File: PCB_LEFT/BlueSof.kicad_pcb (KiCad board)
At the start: 2 copper layers, 134.8 x 98.3 mm, 88 parts, among them J1 USB_C_Receptacle_USB2.0, J12 SM02B-SRSS-TB_LF__SN_, Q2 A03407, SW1 SW_PUSH, SW10 SW_PUSH, SW11 SW_PUSH, SW12 SW_PUSH, SW13 SW_PUSH, SW14 SW_PUSH, SW15 SW_PUSH, SW16 SW_PUSH, SW17 SW_PUSH, SW18 SW_PUSH, SW19 SW_PUSH, SW2 SW_PUSH, SW20 SW_PUSH, SW21 SW_PUSH, SW22 SW_PUSH, SW23 SW_PUSH, SW24 SW_PUSH, SW25 Rotary_Encoder_Switch, SW26 SW_PUSH, SW27 SW_PUSH, SW28 SW_PUSH, SW3 SW_PUSH, SW4 SW_PUSH, SW5 SW_PUSH, SW6 SW_PUSH, SW7 SW_PUSH, SW8 SW_PUSH, SW9 SW_PUSH, U1 LN2054Y42AMR, U2 E73-2G4M08S1C, U3 AP2112K-3.3, Y1 32.768kHz

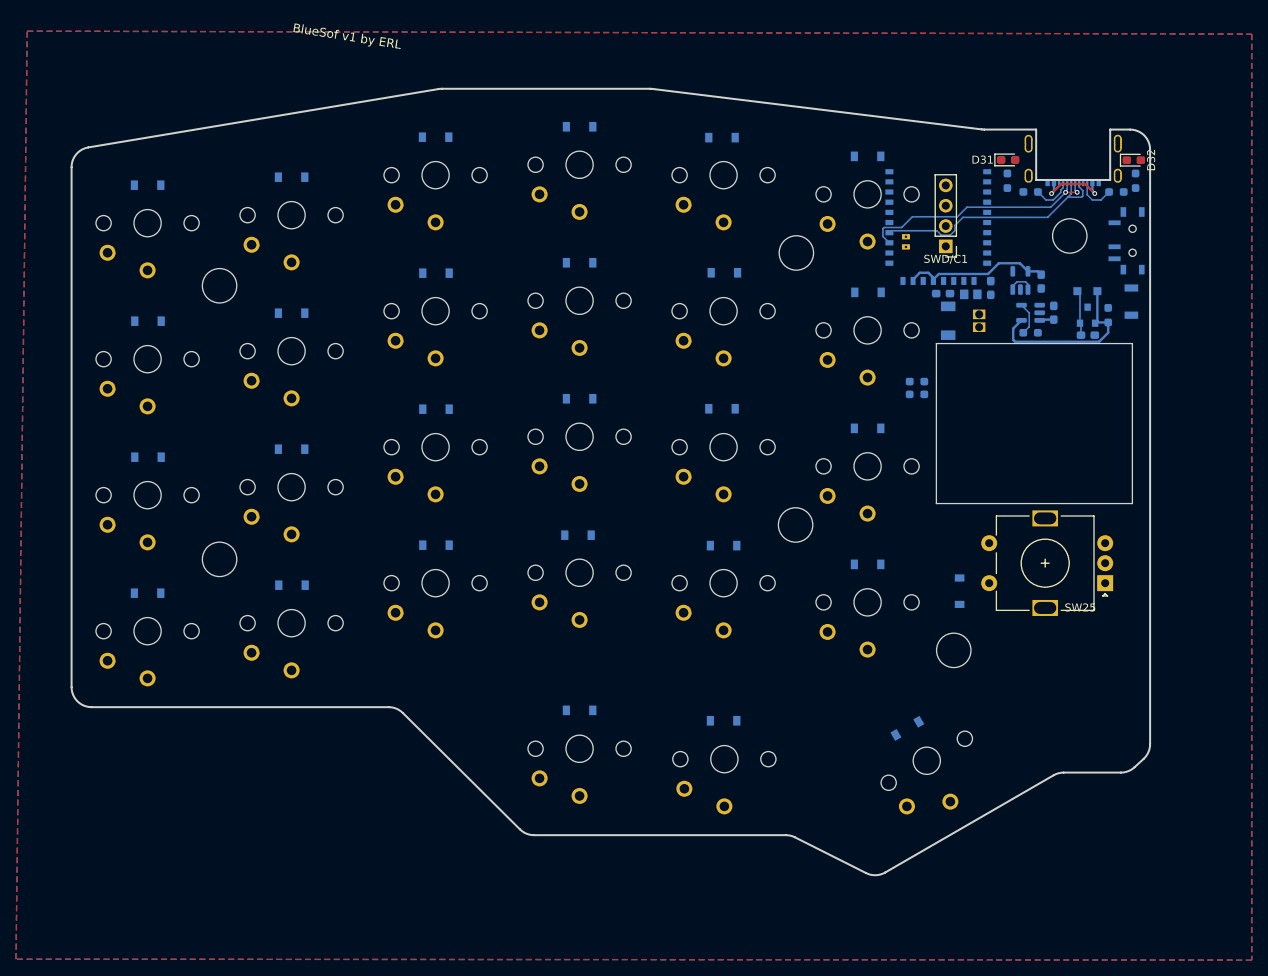
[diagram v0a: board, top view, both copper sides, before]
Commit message: ordered left side from jlc
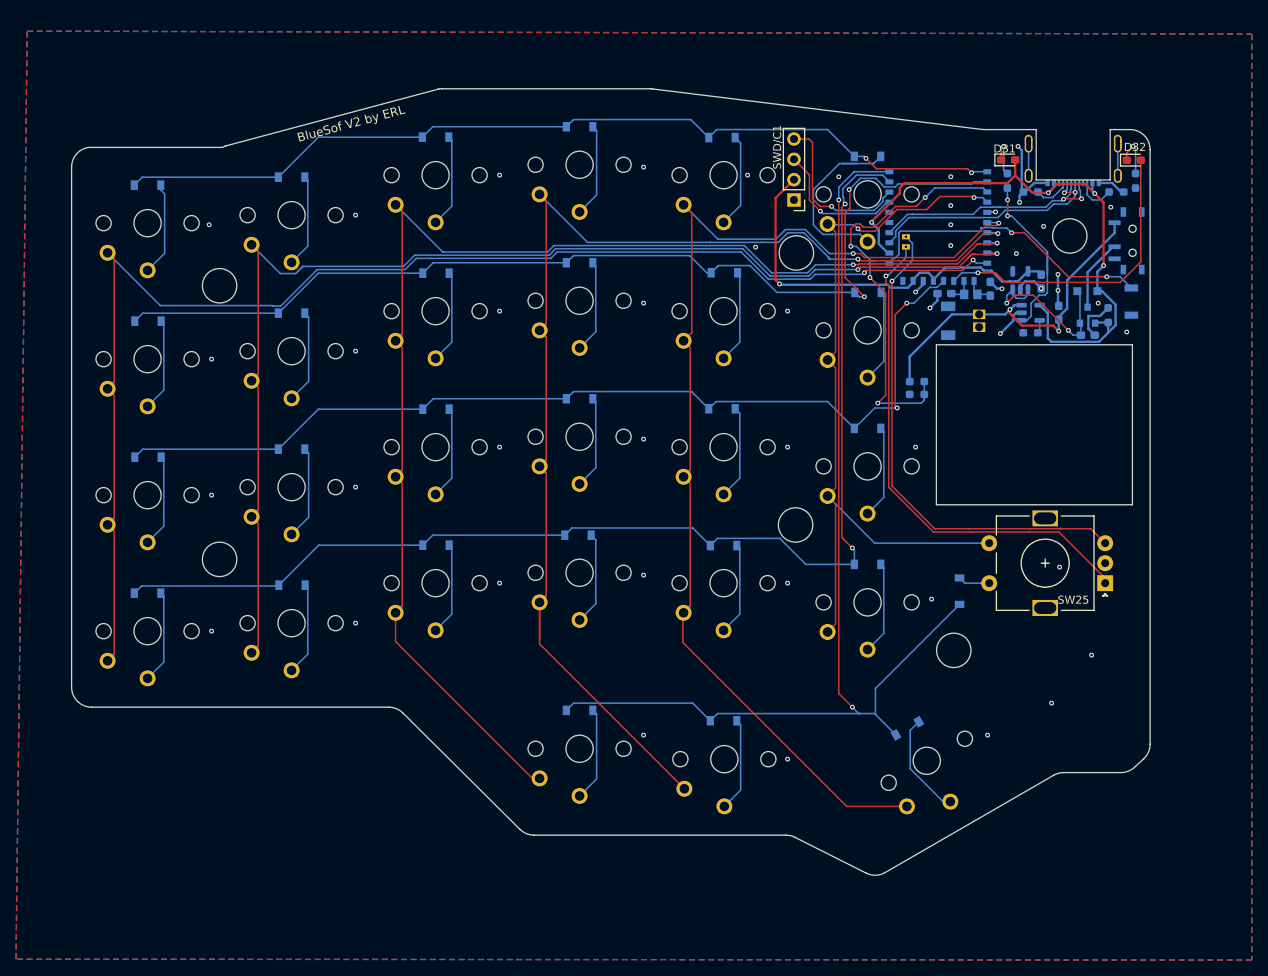
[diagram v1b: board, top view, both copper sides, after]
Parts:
- J12: value SM02B-SRSS-TB_LF__SN_ -> SM02B-SRSS-TB(LF)(SN)
- moved SWD/C1 19.8 mm to (175.7, 54.8)
- moved C4 5.93 mm to (200.2, 65.9), turned to -90 degrees
- moved C3 5.84 mm to (194.5, 66.5), turned to 0 degrees
- moved C1 0.62 mm to (208.8, 68.9)
- turned D7 to 0 degrees
- turned R1 to -90 degrees
- turned R2 to 180 degrees
- turned R6 to -90 degrees
- turned U1 to 0 degrees
- turned Y1 to 0 degrees
- renumbered BATT1 to BATT_SW, RESET1 to RESET
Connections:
- net DATA+ renamed D+
- net DATA- renamed D-
- BATT_SW pad 3: no_connect_72 -> unconnected-(BATT1-Pad3)
- H1 pad 1: Net-(H1-Pad1) -> unconnected-(H1-Pad1)
- H2 pad 1: Net-(H2-Pad1) -> unconnected-(H2-Pad1)
- H3 pad 1: Net-(H3-Pad1) -> unconnected-(H3-Pad1)
- H4 pad 1: Net-(H4-Pad1) -> unconnected-(H4-Pad1)
- H5 pad 1: Net-(H5-Pad1) -> unconnected-(H5-Pad1)
- H6 pad 1: Net-(H6-Pad1) -> unconnected-(H6-Pad1)
- J1 pad A8: no_connect_73 -> unconnected-(J1-PadA8)
- J1 pad B8: no_connect_74 -> unconnected-(J1-PadB8)
- J1 pad S1: GND -> unconnected-(J1-PadS1)
- U2 pad 33: Net-(U2-Pad33) -> unconnected-(U2-Pad33)
- U2 pad 35: Net-(U2-Pad35) -> unconnected-(U2-Pad35)
- U3 pad 4: no_connect_87 -> unconnected-(U3-Pad4)
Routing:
- net col0: track 0.00 -> 171.1 mm, vias 0 -> 2
- net col2: track 0.00 -> 164.4 mm, vias 0 -> 2
- net col1: track 0.00 -> 154.4 mm, vias 0 -> 2
- net col3: track 0.00 -> 154.1 mm, vias 0 -> 2
- net row3: track 0.00 -> 150.8 mm, vias 0 -> 2
- net col4: track 0.00 -> 139.9 mm, vias 0 -> 2
- net row4: track 0.00 -> 136.2 mm, vias 0 -> 2
- net row1: track 0.00 -> 131.0 mm, vias 0 -> 2
- net row2: track 0.00 -> 122.0 mm, vias 0 -> 2
- net row0: track 0.00 -> 113.6 mm, vias 0 -> 2
- net col5: track 0.00 -> 98.5 mm, vias 0 -> 2
- net ENCA: track 0.00 -> 63.7 mm, vias 0 -> 1
- net ENCB: track 0.00 -> 62.3 mm, vias 0 -> 1
- net BATTERY_MEASURE: track 0.00 -> 52.5 mm, vias 0 -> 4
- net VBUS: track 31.7 -> 77.8 mm, vias 2 -> 4
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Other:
- outline, holes or cut-outs redrawn
- board text added: "BlueSof V2 by ERL"
- board text removed: "BlueSof v1 by ERL"
- board text removed: "BlueSof v2 by ERL"

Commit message: minor updates for SMD assembly
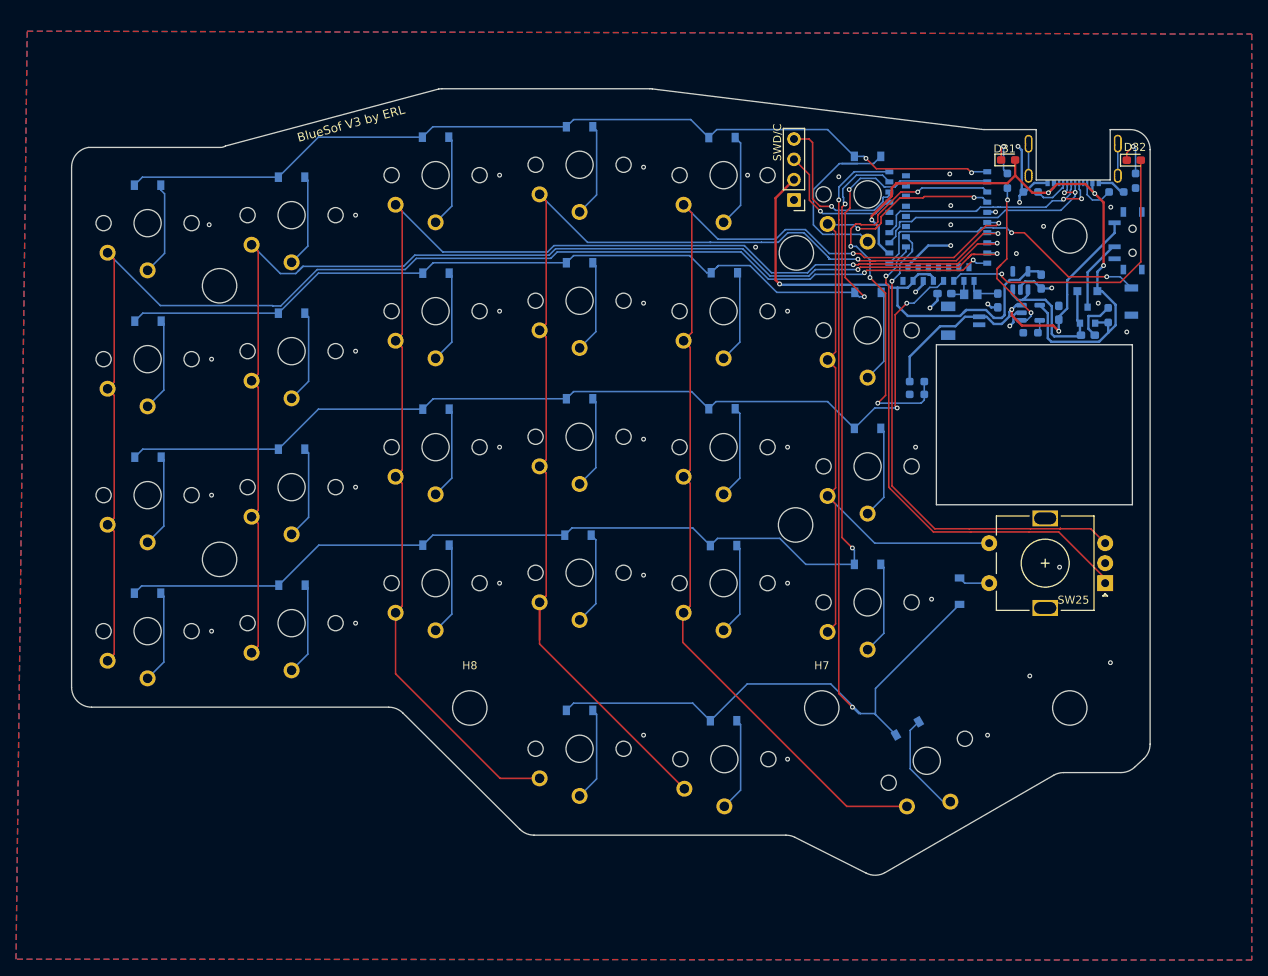
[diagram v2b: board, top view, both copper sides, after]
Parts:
- added H7: MountingHole_Pad, MountingHole:MountingHole_4.3mm_M4, F.Cu at (179.1, 118.3)
- added H8: MountingHole_Pad, MountingHole:MountingHole_4.3mm_M4, F.Cu at (135.1, 118.3)
- U2: footprint BlueSof:E73-2G4M08S1C-52840_minimal_inside_pads -> BlueSof:E73-2G4M08S1C-52840_SMD
- moved H2 16.2 mm to (210.1, 118.3)
- moved C4 1.74 mm to (201.1, 67.4), turned to 90 degrees
- renumbered BATT_SW to BATT1, RESET to RESET1, SWD/C1 to SWD/C
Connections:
- net Net-(C2-Pad1) renamed VIN
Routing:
- net VDD_H: track 51.0 -> 62.1 mm
- net Net-(R1-Pad2): track 23.8 -> 20.4 mm
- net row4: track 136.2 -> 139.3 mm
- net VBUS: track 77.8 -> 80.2 mm
- net col2: track 164.4 -> 166.8 mm
- net VIN: track 23.0 -> 20.7 mm, vias 2 -> 0
- net GND: track 38.7 -> 40.8 mm, vias 49 -> 47
- net col5: track 98.5 -> 100.0 mm
- net D+: track 30.6 -> 31.6 mm
- net VBAT: track 43.8 -> 44.8 mm
- net Net-(C4-Pad2): track 3.53 -> 4.07 mm
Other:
- board text added: "BlueSof V3 by ERL"
- board text removed: "BlueSof V2 by ERL"

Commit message: working towards next order
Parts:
- added Batt: Jumper_2_Open, Jumper:SolderJumper-2_P1.3mm_Open_Pad1.0x1.5mm, B.Cu at (190.9, 73.8)
- added J2: Conn_01x01_Male, Connector_PinSocket_1.27mm:PinSocket_1x01_P1.27mm_Vertical, F.Cu at (175.9, 80.1)
- added J3: Conn_01x01_Male, Connector_PinSocket_1.27mm:PinSocket_1x01_P1.27mm_Vertical, F.Cu at (175.9, 76.5)
- C1, C2, C3, C4, C5: footprint Capacitor_SMD:C_0603_1608Metric_Pad1.08x0.95mm_HandSolder -> Capacitor_SMD:C_0603_1608Metric
- D31, D32: footprint LED_SMD:LED_0603_1608Metric_Pad1.05x0.95mm_HandSolder -> LED_SMD:LED_0603_1608Metric
- R1, R2, R4, R5, R6, R7, R8, R9: footprint Resistor_SMD:R_0603_1608Metric_Pad0.98x0.95mm_HandSolder -> Resistor_SMD:R_0603_1608Metric
- renumbered SWD/C to SWD/C1
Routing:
- net Net-(J3-Pad1): track 0.00 -> 17.6 mm
- net GND: track 40.8 -> 42.0 mm, vias 47 -> 48
- net row2: track 122.0 -> 122.8 mm
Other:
- board text added: "BATT"
